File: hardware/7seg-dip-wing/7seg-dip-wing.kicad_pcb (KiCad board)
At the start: 2 copper layers, 53 x 22.9 mm, 10 parts, among them J1 Feather, SW1 SW_DIP_x08, U1 LTD-5623Ax, U2 74LVC2G17

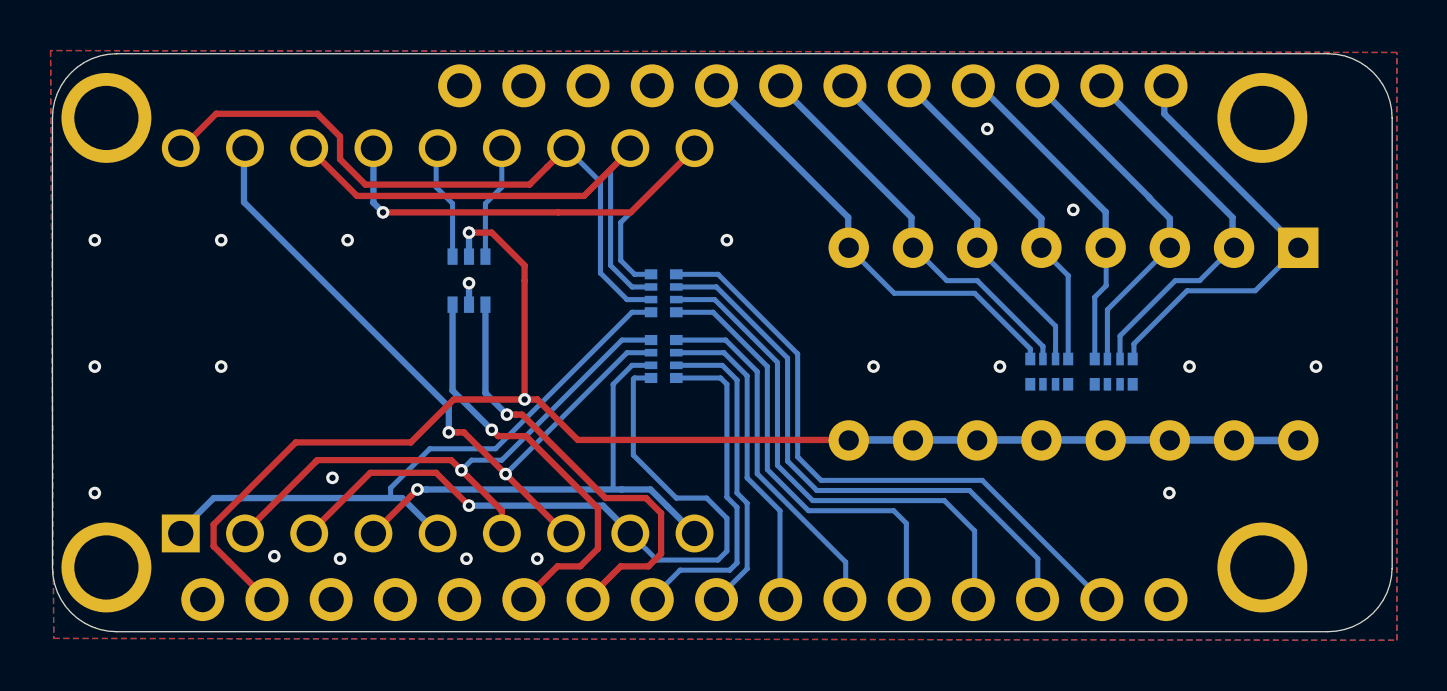
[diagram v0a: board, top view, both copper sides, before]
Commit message: changes to make everything work with new library setup
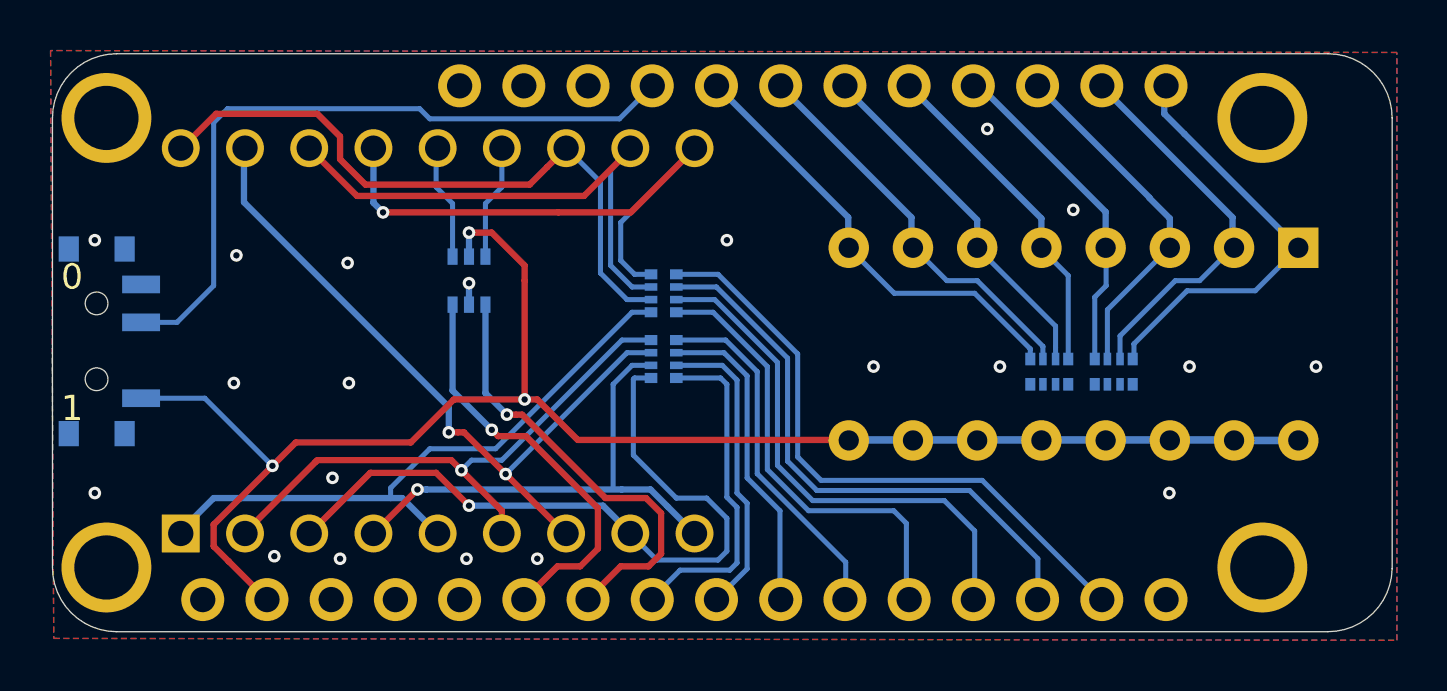
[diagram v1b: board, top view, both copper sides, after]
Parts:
- removed the REF** at (52.3, 59.8)
- added SW2: SW_SPDT, josh-footprints:SW_SPDT_PCM12, B.Cu at (47.9, 59.0)
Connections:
- J1 pad 25: (no net) -> /SWITCH
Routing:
- net /SWITCH: track 0.00 -> 28.2 mm
- net +3V3: track 58.5 -> 64.8 mm, vias 2 -> 3
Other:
- net class Default: clearance 0.2 -> 0.15; trace_width 0.2 -> 0.15
- rule trace_clearance: 0.2 -> 0.15
- board text added: "0"
- board text added: "1"

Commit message: fixing things which broke resulting from library change
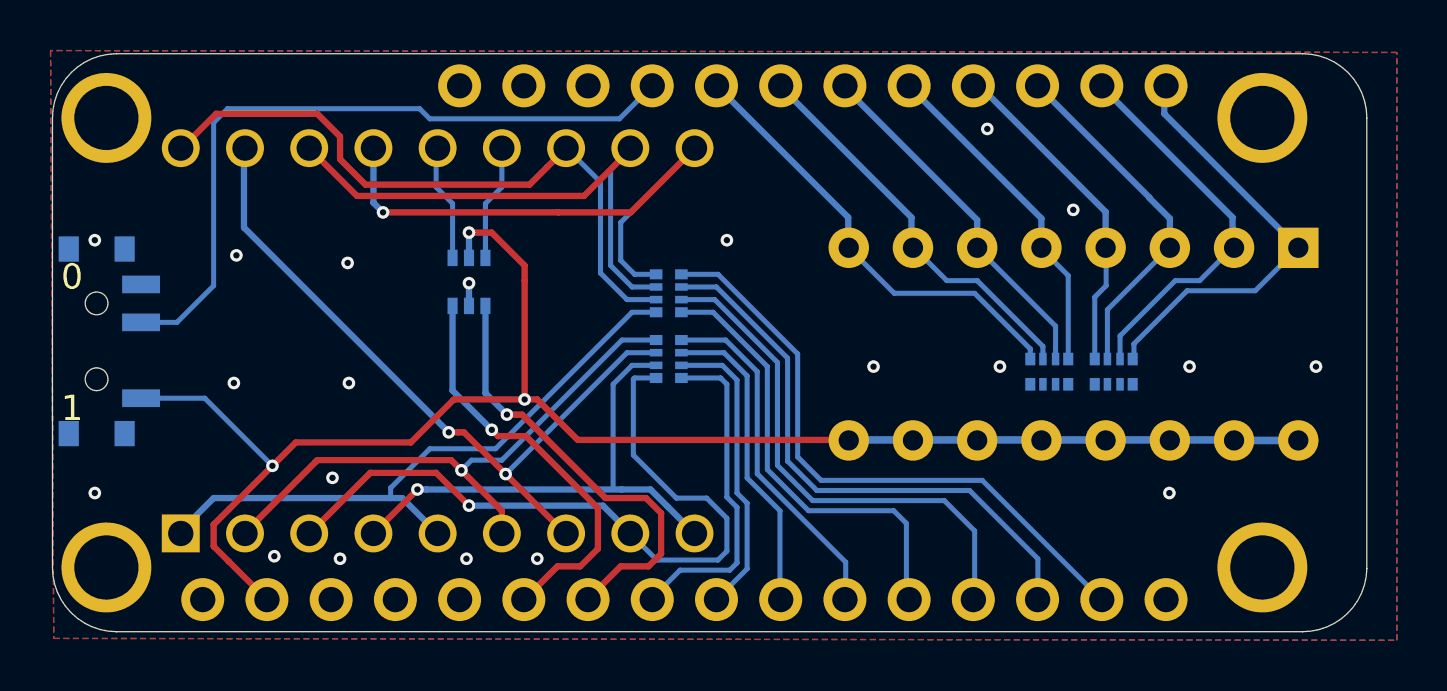
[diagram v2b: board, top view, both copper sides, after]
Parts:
- J1: footprint josh-footprints:PCB_FeatherWing -> josh-connectors:featherwing
- SW2: footprint josh-footprints:SW_SPDT_PCM12 -> josh-buttons-switches:SW_SPDT_PCM12
- U1: footprint Display_7Segment:DA56-11SURKWA -> Display_7Segment:DA56-11SEKWA
- moved RN3 2.61 mm to (70.2, 57.1), turned to 180 degrees
- moved RN4 2.61 mm to (70.2, 59.7), turned to 180 degrees
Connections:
- J1 pad 1: (no net) -> Net-(J1-Pad1)
- J1 pad 10: /SEG_B -> /SEG_G
- J1 pad 11: /SEG_A -> /SEG_D
- J1 pad 12: /SEG_DP -> /SEG_E
- J1 pad 13: /SEG_G -> /SEG_F
- J1 pad 14: /SEG_F -> /SEG_A
- J1 pad 15: /SEG_E -> /SEG_B
- J1 pad 26: (no net) -> Net-(J1-Pad26)
- J1 pad 27: (no net) -> Net-(J1-Pad27)
- J1 pad 28: (no net) -> Net-(J1-Pad28)
- J1 pad 3: (no net) -> Net-(J1-Pad3)
- J1 pad 5: (no net) -> Net-(J1-Pad5)
- J1 pad 8: /SEG_D -> /SEG_C
- J1 pad 9: /SEG_C -> /SEG_DP
- RN3 pad 1: Net-(RN3-Pad1) -> /SEG_B
- RN3 pad 2: Net-(RN3-Pad2) -> /SEG_A
- RN3 pad 3: Net-(RN3-Pad3) -> /SEG_F
- RN3 pad 4: Net-(RN3-Pad4) -> /SEG_E
- RN3 pad 5: /SEG_A -> Net-(RN3-Pad5)
- RN3 pad 6: /SEG_B -> Net-(RN3-Pad6)
- RN3 pad 7: /SEG_C -> Net-(RN3-Pad7)
- RN3 pad 8: /SEG_D -> Net-(RN3-Pad8)
- RN4 pad 1: Net-(RN4-Pad1) -> /SEG_D
- RN4 pad 2: Net-(RN4-Pad2) -> /SEG_G
- RN4 pad 3: Net-(RN4-Pad3) -> /SEG_DP
- RN4 pad 4: Net-(RN4-Pad4) -> /SEG_C
- RN4 pad 5: /SEG_E -> Net-(RN4-Pad5)
- RN4 pad 6: /SEG_F -> Net-(RN4-Pad6)
- RN4 pad 7: /SEG_G -> Net-(RN4-Pad7)
- RN4 pad 8: /SEG_DP -> Net-(RN4-Pad8)
- U1 pad 1: Net-(RN4-Pad1) -> Net-(RN3-Pad5)
- U1 pad 10: Net-(RN4-Pad4) -> Net-(RN3-Pad8)
- U1 pad 11: Net-(RN4-Pad3) -> Net-(RN3-Pad7)
- U1 pad 12: Net-(RN4-Pad2) -> Net-(RN3-Pad6)
- U1 pad 15: Net-(RN4-Pad4) -> Net-(RN3-Pad8)
- U1 pad 16: Net-(RN4-Pad3) -> Net-(RN3-Pad7)
- U1 pad 17: Net-(RN3-Pad3) -> Net-(RN4-Pad7)
- U1 pad 18: Net-(RN4-Pad2) -> Net-(RN3-Pad6)
- U1 pad 2: Net-(RN3-Pad4) -> Net-(RN4-Pad8)
- U1 pad 3: Net-(RN3-Pad1) -> Net-(RN4-Pad5)
- U1 pad 4: Net-(RN3-Pad2) -> Net-(RN4-Pad6)
- U1 pad 5: Net-(RN4-Pad1) -> Net-(RN3-Pad5)
- U1 pad 6: Net-(RN3-Pad4) -> Net-(RN4-Pad8)
- U1 pad 7: Net-(RN3-Pad3) -> Net-(RN4-Pad7)
- U1 pad 8: Net-(RN3-Pad1) -> Net-(RN4-Pad5)
- U1 pad 9: Net-(RN3-Pad2) -> Net-(RN4-Pad6)
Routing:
- net Net-(RN4-Pad5): track 0.00 -> 28.9 mm, vias 0 -> 1
- net Net-(RN3-Pad1): track 28.9 -> 0.00 mm, vias 1 -> 0
- net Net-(RN4-Pad7): track 0.00 -> 28.6 mm, vias 0 -> 2
- net Net-(RN3-Pad3): track 28.6 -> 0.00 mm, vias 2 -> 0
- net Net-(RN4-Pad2): track 26.0 -> 0.00 mm
- net Net-(RN3-Pad6): track 0.00 -> 26.0 mm
- net Net-(RN4-Pad1): track 24.9 -> 0.00 mm
- net Net-(RN3-Pad5): track 0.00 -> 24.9 mm
- net Net-(RN4-Pad4): track 23.2 -> 0.00 mm, vias 1 -> 0
- net Net-(RN3-Pad8): track 0.00 -> 23.2 mm, vias 0 -> 1
- net Net-(RN4-Pad8): track 0.00 -> 22.8 mm, vias 0 -> 1
- net Net-(RN3-Pad4): track 22.8 -> 0.00 mm, vias 1 -> 0
- net Net-(RN4-Pad3): track 21.2 -> 0.00 mm
- net Net-(RN3-Pad7): track 0.00 -> 21.2 mm
- net Net-(RN4-Pad6): track 0.00 -> 20.5 mm, vias 0 -> 1
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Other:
- board size 53 x 22.9 mm -> 52 x 22.9 mm

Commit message: generated gerbers, changed pin labelling to match constraints file
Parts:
- added REF**: Josh Details, josh-logos:josh-details, B.Cu at (86.2, 51.4)
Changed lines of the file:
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@@
     (tracks 284)
     (zones 0)
-    (modules 10)
+    (modules 11)
     (nets 38)
   )
@@
       (outputformat 1)
       (mirror false)
-      (drillshape 1)
+      (drillshape 0)
       (scaleselection 1)
-      (outputdirectory ""))
+      (outputdirectory "gerbers/"))
   )
   (net 0 "")
@@
     (add_net "Net-(U1-Pad14)")
   )
+  (module josh-logos:josh-details (layer B.Cu)
+    (at 86.25 51.4 180)
+    (fp_text reference REF** (at 0 5.6) (layer B.Fab)
+      (effects (font (size 1 1) (thickness 0.15)) (justify mirror))
+    )
+    (fp_text value "Josh Details" (at 0 6.6) (layer B.Fab)
+      (effects (font (size 1 1) (thickness 0.15)) (justify mirror))
+    )
+    (fp_text user github.com/joshajohnson (at 4.6736 -2.032) (layer B.SilkS)
+      (effects (font (size 1 1) (thickness 0.15)) (justify mirror))
+    )
+    (fp_text user joshajohnson.com (at 2 -0.5) (layer B.SilkS)
+      (effects (font (size 1 1) (thickness 0.15)) (justify mirror))
+    )
+    (fp_text user "Josh Johnson" (at 0.2 1 180) (layer B.SilkS)
+      (effects (font (size 1 1) (thickness 0.15)) (justify mirror))
+    )
+  )
   (module Display_7Segment:DA56-11SEKWA (layer F.Cu)
     (at 50.9 66.6 90)
@@
     )
     (fp_text value "Josh Details" (at 0 6.6) (layer B.Fab)
-      (effects (font (size 1 1) (thickness 0.15)) (justify mirror))
-    )
-    (fp_text user github.com/joshajohnson/iCE40-fpga (at 9.6 -2) (layer B.SilkS)
-      (effects (font (size 1 1) (thickness 0.15)) (justify mirror))
-    )
-    (fp_text user joshajohnson.com (at 2 -0.5) (layer B.SilkS)
-      (effects (font (size 1 1) (thickness 0.15)) (justify mirror))
-    )
-    (fp_text user "Josh Johnson" (at 0.2 1 180) (layer B.SilkS)
       (effects (font (size 1 1) (thickness 0.15)) (justify mirror))
     )
@@
   (segment (start 92.5 55.3) (end 92.5 54.1) (width 0.25) (layer B.Cu) (net 8))
   (segment (start 92.5 54.1) (end 87.4 49) (width 0.25) (layer B.Cu) (net 8))
+  (segment (start 74.900066 63.740166) (end 76.059911 64.900011) (width 0.2) (layer B.Cu) (net 9))
+  (segment (start 82.100011 64.900011) (end 84.8 67.6) (width 0.2) (layer B.Cu) (net 9))
+  (segment (start 70.6 56.85) (end 72.0843 56.85) (width 0.2) (layer B.Cu) (net 9))
+  (segment (start 84.8 67.6) (end 84.8 69.2) (width 0.2) (layer B.Cu) (net 9))
+  (segment (start 72.0843 56.85) (end 74.900066 59.665766) (width 0.2) (layer B.Cu) (net 9))
+  (segment (start 76.059911 64.900011) (end 82.100011 64.900011) (width 0.2) (layer B.Cu) (net 9))
+  (segment (start 74.900066 59.665766) (end 74.900066 63.740166) (width 0.2) (layer B.Cu) (net 9))
+  (segment (start 72.615688 68.050012) (end 70.649988 68.050012) (width 0.2) (layer B.Cu) (net 10))
+  (segment (start 72.25 60.45) (end 72.5 60.7) (width 0.2) (layer B.Cu) (net 10))
+  (segment (start 72.5 60.7) (end 72.5 65.1657) (width 0.2) (layer B.Cu) (net 10))
+  (segment (start 70.649988 68.050012) (end 69.5 69.2) (width 0.2) (layer B.Cu) (net 10))
+  (segment (start 72.5 65.1657) (end 72.900011 65.565711) (width 0.2) (layer B.Cu) (net 10))
+  (segment (start 72.900011 65.565711) (end 72.900011 67.765689) (width 0.2) (layer B.Cu) (net 10))
+  (segment (start 70.6 60.45) (end 72.25 60.45) (width 0.2) (layer B.Cu) (net 10))
+  (segment (start 72.900011 67.765689) (end 72.615688 68.050012) (width 0.2) (layer B.Cu) (net 10))
+  (segment (start 72.15 56.35) (end 75.300077 59.500077) (width 0.2) (layer B.Cu) (net 11))
+  (segment (start 75.300077 59.500077) (end 75.300077 63.574477) (width 0.2) (layer B.Cu) (net 11))
+  (segment (start 75.300077 63.574477) (end 76.2256 64.5) (width 0.2) (layer B.Cu) (net 11))
+  (segment (start 70.6 56.35) (end 72.15 56.35) (width 0.2) (layer B.Cu) (net 11))
+  (segment (start 76.2256 64.5) (end 82.6 64.5) (width 0.2) (layer B.Cu) (net 11))
+  (segment (start 82.6 64.5) (end 87.3 69.2) (width 0.2) (layer B.Cu) (net 11))
   (segment (start 72.45 58.95) (end 73.700033 60.200033) (width 0.2) (layer B.Cu) (net 12))
   (segment (start 73.700033 64.237233) (end 77.2 67.7372) (width 0.2) (layer B.Cu) (net 12))
@@
   (segment (start 73.300022 65.400022) (end 73.300022 67.999978) (width 0.2) (layer B.Cu) (net 13))
   (segment (start 72.900011 60.531411) (end 72.900011 65.000011) (width 0.2) (layer B.Cu) (net 13))
+  (segment (start 82.3 66.5) (end 82.3 69.3) (width 0.2) (layer B.Cu) (net 14))
+  (segment (start 72.0186 57.35) (end 74.500055 59.831455) (width 0.2) (layer B.Cu) (net 14))
+  (segment (start 74.500055 59.831455) (end 74.500055 63.905855) (width 0.2) (layer B.Cu) (net 14))
+  (segment (start 74.500055 63.905855) (end 75.894222 65.300022) (width 0.2) (layer B.Cu) (net 14))
+  (segment (start 75.894222 65.300022) (end 81.100022 65.300022) (width 0.2) (layer B.Cu) (net 14))
+  (segment (start 70.6 57.35) (end 72.0186 57.35) (width 0.2) (layer B.Cu) (net 14))
+  (segment (start 81.100022 65.300022) (end 82.3 66.5) (width 0.2) (layer B.Cu) (net 14))
   (segment (start 73.300022 60.365722) (end 73.300022 64.402922) (width 0.2) (layer B.Cu) (net 15))
   (segment (start 72.3843 59.45) (end 73.300022 60.365722) (width 0.2) (layer B.Cu) (net 15))
@@
   (segment (start 74.6 65.7029) (end 74.6 69.2) (width 0.2) (layer B.Cu) (net 15))
   (segment (start 70.6 59.45) (end 72.3843 59.45) (width 0.2) (layer B.Cu) (net 15))
-  (segment (start 72.615688 68.050012) (end 70.649988 68.050012) (width 0.2) (layer B.Cu) (net 10))
-  (segment (start 72.25 60.45) (end 72.5 60.7) (width 0.2) (layer B.Cu) (net 10))
-  (segment (start 72.5 60.7) (end 72.5 65.1657) (width 0.2) (layer B.Cu) (net 10))
-  (segment (start 70.649988 68.050012) (end 69.5 69.2) (width 0.2) (layer B.Cu) (net 10))
-  (segment (start 72.5 65.1657) (end 72.900011 65.565711) (width 0.2) (layer B.Cu) (net 10))
-  (segment (start 72.900011 65.565711) (end 72.900011 67.765689) (width 0.2) (layer B.Cu) (net 10))
-  (segment (start 70.6 60.45) (end 72.25 60.45) (width 0.2) (layer B.Cu) (net 10))
-  (segment (start 72.900011 67.765689) (end 72.615688 68.050012) (width 0.2) (layer B.Cu) (net 10))
   (segment (start 79.6 66.2) (end 79.6 69.1) (width 0.2) (layer B.Cu) (net 16))
   (segment (start 79.6 69.1) (end 79.7 69.2) (width 0.2) (layer B.Cu) (net 16))
@@
   (segment (start 71.9529 57.85) (end 74.100044 59.997144) (width 0.2) (layer B.Cu) (net 16))
   (segment (start 70.6 57.85) (end 71.9529 57.85) (width 0.2) (layer B.Cu) (net 16))
-  (segment (start 74.900066 63.740166) (end 76.059911 64.900011) (width 0.2) (layer B.Cu) (net 9))
-  (segment (start 82.100011 64.900011) (end 84.8 67.6) (width 0.2) (layer B.Cu) (net 9))
-  (segment (start 70.6 56.85) (end 72.0843 56.85) (width 0.2) (layer B.Cu) (net 9))
-  (segment (start 84.8 67.6) (end 84.8 69.2) (width 0.2) (layer B.Cu) (net 9))
-  (segment (start 72.0843 56.85) (end 74.900066 59.665766) (width 0.2) (layer B.Cu) (net 9))
-  (segment (start 76.059911 64.900011) (end 82.100011 64.900011) (width 0.2) (layer B.Cu) (net 9))
-  (segment (start 74.900066 59.665766) (end 74.900066 63.740166) (width 0.2) (layer B.Cu) (net 9))
-  (segment (start 82.3 66.5) (end 82.3 69.3) (width 0.2) (layer B.Cu) (net 14))
-  (segment (start 72.0186 57.35) (end 74.500055 59.831455) (width 0.2) (layer B.Cu) (net 14))
-  (segment (start 74.500055 59.831455) (end 74.500055 63.905855) (width 0.2) (layer B.Cu) (net 14))
-  (segment (start 74.500055 63.905855) (end 75.894222 65.300022) (width 0.2) (layer B.Cu) (net 14))
-  (segment (start 75.894222 65.300022) (end 81.100022 65.300022) (width 0.2) (layer B.Cu) (net 14))
-  (segment (start 70.6 57.35) (end 72.0186 57.35) (width 0.2) (layer B.Cu) (net 14))
-  (segment (start 81.100022 65.300022) (end 82.3 66.5) (width 0.2) (layer B.Cu) (net 14))
-  (segment (start 72.15 56.35) (end 75.300077 59.500077) (width 0.2) (layer B.Cu) (net 11))
-  (segment (start 75.300077 59.500077) (end 75.300077 63.574477) (width 0.2) (layer B.Cu) (net 11))
-  (segment (start 75.300077 63.574477) (end 76.2256 64.5) (width 0.2) (layer B.Cu) (net 11))
-  (segment (start 70.6 56.35) (end 72.15 56.35) (width 0.2) (layer B.Cu) (net 11))
-  (segment (start 76.2256 64.5) (end 82.6 64.5) (width 0.2) (layer B.Cu) (net 11))
-  (segment (start 82.6 64.5) (end 87.3 69.2) (width 0.2) (layer B.Cu) (net 11))
   (segment (start 63.6 52.9) (end 63.6 51.4) (width 0.2) (layer B.Cu) (net 17))
   (segment (start 62.95 55.65) (end 62.95 53.55) (width 0.2) (layer B.Cu) (net 17))
